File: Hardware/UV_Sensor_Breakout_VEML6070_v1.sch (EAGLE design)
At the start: 7 parts, among them U1 VEML6070

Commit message: Minor fixes
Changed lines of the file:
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@@
 <grid distance="0.1" unitdist="inch" unit="inch" style="lines" multiple="1" display="no" altdistance="0.01" altunitdist="inch" altunit="inch"/>
 <layers>
-<layer number="1" name="Top" color="4" fill="1" visible="yes" active="no"/>
-<layer number="16" name="Bottom" color="1" fill="1" visible="yes" active="no"/>
-<layer number="17" name="Pads" color="2" fill="1" visible="yes" active="no"/>
-<layer number="18" name="Vias" color="2" fill="1" visible="yes" active="no"/>
-<layer number="19" name="Unrouted" color="6" fill="1" visible="yes" active="no"/>
-<layer number="20" name="Dimension" color="15" fill="1" visible="yes" active="no"/>
-<layer number="21" name="tPlace" color="24" fill="1" visible="yes" active="no"/>
-<layer number="22" name="bPlace" color="13" fill="1" visible="yes" active="no"/>
-<layer number="23" name="tOrigins" color="15" fill="1" visible="yes" active="no"/>
-<layer number="24" name="bOrigins" color="15" fill="1" visible="yes" active="no"/>
-<layer number="25" name="tNames" color="31" fill="1" visible="yes" active="no"/>
-<layer number="26" name="bNames" color="23" fill="1" visible="yes" active="no"/>
-<layer number="27" name="tValues" color="30" fill="1" visible="yes" active="no"/>
-<layer number="28" name="bValues" color="20" fill="1" visible="yes" active="no"/>
+<layer number="1" name="Top" color="4" fill="1" visible="no" active="no"/>
+<layer number="16" name="Bottom" color="1" fill="1" visible="no" active="no"/>
+<layer number="17" name="Pads" color="2" fill="1" visible="no" active="no"/>
+<layer number="18" name="Vias" color="2" fill="1" visible="no" active="no"/>
+<layer number="19" name="Unrouted" color="6" fill="1" visible="no" active="no"/>
+<layer number="20" name="Dimension" color="15" fill="1" visible="no" active="no"/>
+<layer number="21" name="tPlace" color="24" fill="1" visible="no" active="no"/>
+<layer number="22" name="bPlace" color="13" fill="1" visible="no" active="no"/>
+<layer number="23" name="tOrigins" color="15" fill="1" visible="no" active="no"/>
+<layer number="24" name="bOrigins" color="15" fill="1" visible="no" active="no"/>
+<layer number="25" name="tNames" color="31" fill="1" visible="no" active="no"/>
+<layer number="26" name="bNames" color="23" fill="1" visible="no" active="no"/>
+<layer number="27" name="tValues" color="30" fill="1" visible="no" active="no"/>
+<layer number="28" name="bValues" color="20" fill="1" visible="no" active="no"/>
 <layer number="29" name="tStop" color="7" fill="3" visible="no" active="no"/>
 <layer number="30" name="bStop" color="7" fill="6" visible="no" active="no"/>
@@
 <layer number="35" name="tGlue" color="7" fill="4" visible="no" active="no"/>
 <layer number="36" name="bGlue" color="7" fill="5" visible="no" active="no"/>
-<layer number="37" name="tTest" color="7" fill="1" visible="yes" active="no"/>
-<layer number="38" name="bTest" color="7" fill="1" visible="yes" active="no"/>
+<layer number="37" name="tTest" color="7" fill="1" visible="no" active="no"/>
+<layer number="38" name="bTest" color="7" fill="1" visible="no" active="no"/>
 <layer number="39" name="tKeepout" color="4" fill="11" visible="no" active="no"/>
 <layer number="40" name="bKeepout" color="1" fill="11" visible="no" active="no"/>
@@
 <layer number="44" name="Drills" color="7" fill="1" visible="no" active="no"/>
 <layer number="45" name="Holes" color="7" fill="1" visible="no" active="no"/>
-<layer number="46" name="Milling" color="3" fill="1" visible="yes" active="no"/>
-<layer number="47" name="Measures" color="7" fill="1" visible="yes" active="no"/>
-<layer number="48" name="Document" color="17" fill="1" visible="yes" active="no"/>
-<layer number="49" name="Reference" color="7" fill="1" visible="yes" active="no"/>
-<layer number="50" name="dxf" color="7" fill="1" visible="yes" active="no"/>
-<layer number="51" name="tDocu" color="27" fill="1" visible="yes" active="no"/>
-<layer number="52" name="bDocu" color="19" fill="1" visible="yes" active="no"/>
-<layer number="53" name="tGND_GNDA" color="7" fill="9" visible="yes" active="no"/>
-<layer number="54" name="bGND_GNDA" color="1" fill="9" visible="yes" active="no"/>
-<layer number="56" name="wert" color="7" fill="1" visible="yes" active="no"/>
-<layer number="57" name="tCAD" color="7" fill="1" visible="yes" active="no"/>
+<layer number="46" name="Milling" color="3" fill="1" visible="no" active="no"/>
+<layer number="47" name="Measures" color="7" fill="1" visible="no" active="no"/>
+<layer number="48" name="Document" color="17" fill="1" visible="no" active="no"/>
+<layer number="49" name="Reference" color="7" fill="1" visible="no" active="no"/>
+<layer number="50" name="dxf" color="7" fill="1" visible="no" active="no"/>
+<layer number="51" name="tDocu" color="27" fill="1" visible="no" active="no"/>
+<layer number="52" name="bDocu" color="19" fill="1" visible="no" active="no"/>
+<layer number="53" name="tGND_GNDA" color="7" fill="9" visible="no" active="no"/>
+<layer number="54" name="bGND_GNDA" color="1" fill="9" visible="no" active="no"/>
+<layer number="56" name="wert" color="7" fill="1" visible="no" active="no"/>
+<layer number="57" name="tCAD" color="7" fill="1" visible="no" active="no"/>
 <layer number="90" name="Modules" color="5" fill="1" visible="yes" active="yes"/>
 <layer number="91" name="Nets" color="2" fill="1" visible="yes" active="yes"/>
@@
 <pinref part="U1" gate="U" pin="ACK"/>
 <wire x1="2.54" y1="5.08" x2="10.16" y2="5.08" width="0.1524" layer="91"/>
-<label x="25.4" y="5.08" size="1.27" layer="95" xref="yes"/>
 <label x="5.588" y="5.334" size="1.27" layer="95"/>
 </segment>

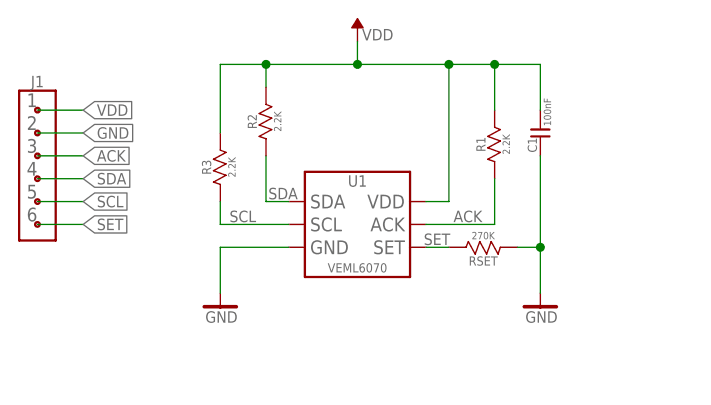
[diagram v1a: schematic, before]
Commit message: Legend added
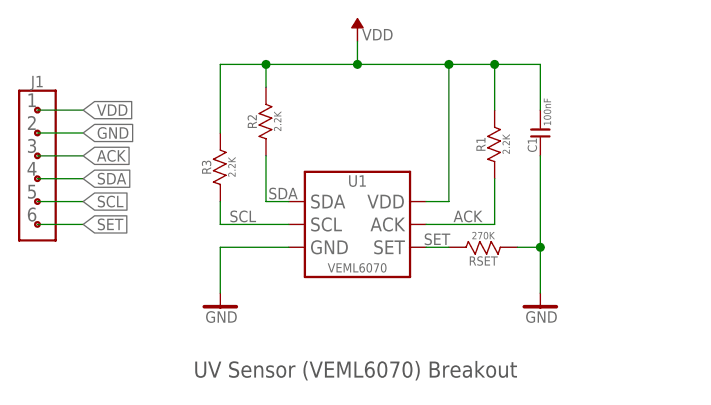
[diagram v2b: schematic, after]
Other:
- note added: "UV Sensor (VEML6070) Breakout"
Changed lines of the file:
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@@
 <sheet>
 <plain>
+<text x="12.7" y="-10.16" size="1.778" layer="97" rot="R180">UV Sensor (VEML6070) Breakout </text>
 </plain>
 <instances>
